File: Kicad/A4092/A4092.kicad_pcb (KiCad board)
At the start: 4 copper layers, 175.6 x 122.1 mm, 127 parts, among them CN1 Zorro3, J1 5749721-7, J2 5749721-7, J3 TO-LED, J4 TO-MB, J5 TO-A3000-LED, J6 TO-A3000-MB, J8 Conn_01x06_Pin, U1 SN74ABT16543DGGR, U10 DS21S07A, U11 DS21S07A, U12 DS21S07A, U13 W25X40CLSN, U2 SN74ABT16543DGGR, U3 SN74ABT16543DGGR, U4 SN74ABT16543DGGR, U5 74LVC07APW_118, U6 SN74ABT16245ADGGR, U7 AMS1117-3.3, U8 XC95144XL-TQ144, U9 LSI53C770 SCSI Host Controller, Y1 Abracon ACO-50MHz, Y2 Abracon ACO-40MHz

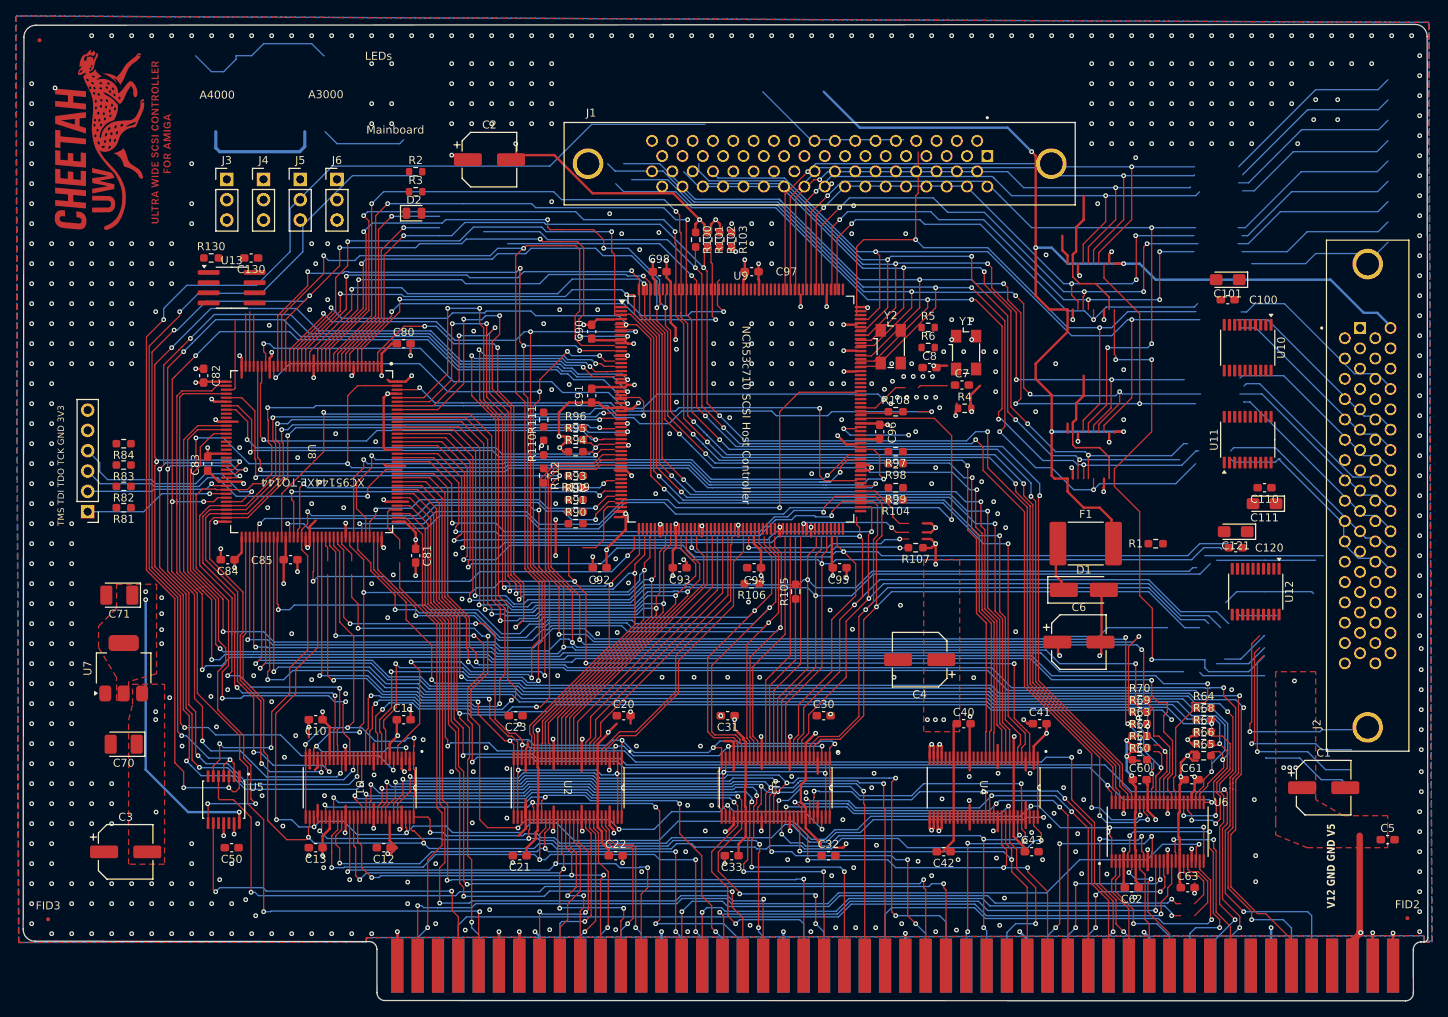
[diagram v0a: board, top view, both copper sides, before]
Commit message: Placement updates -SCSI moved south
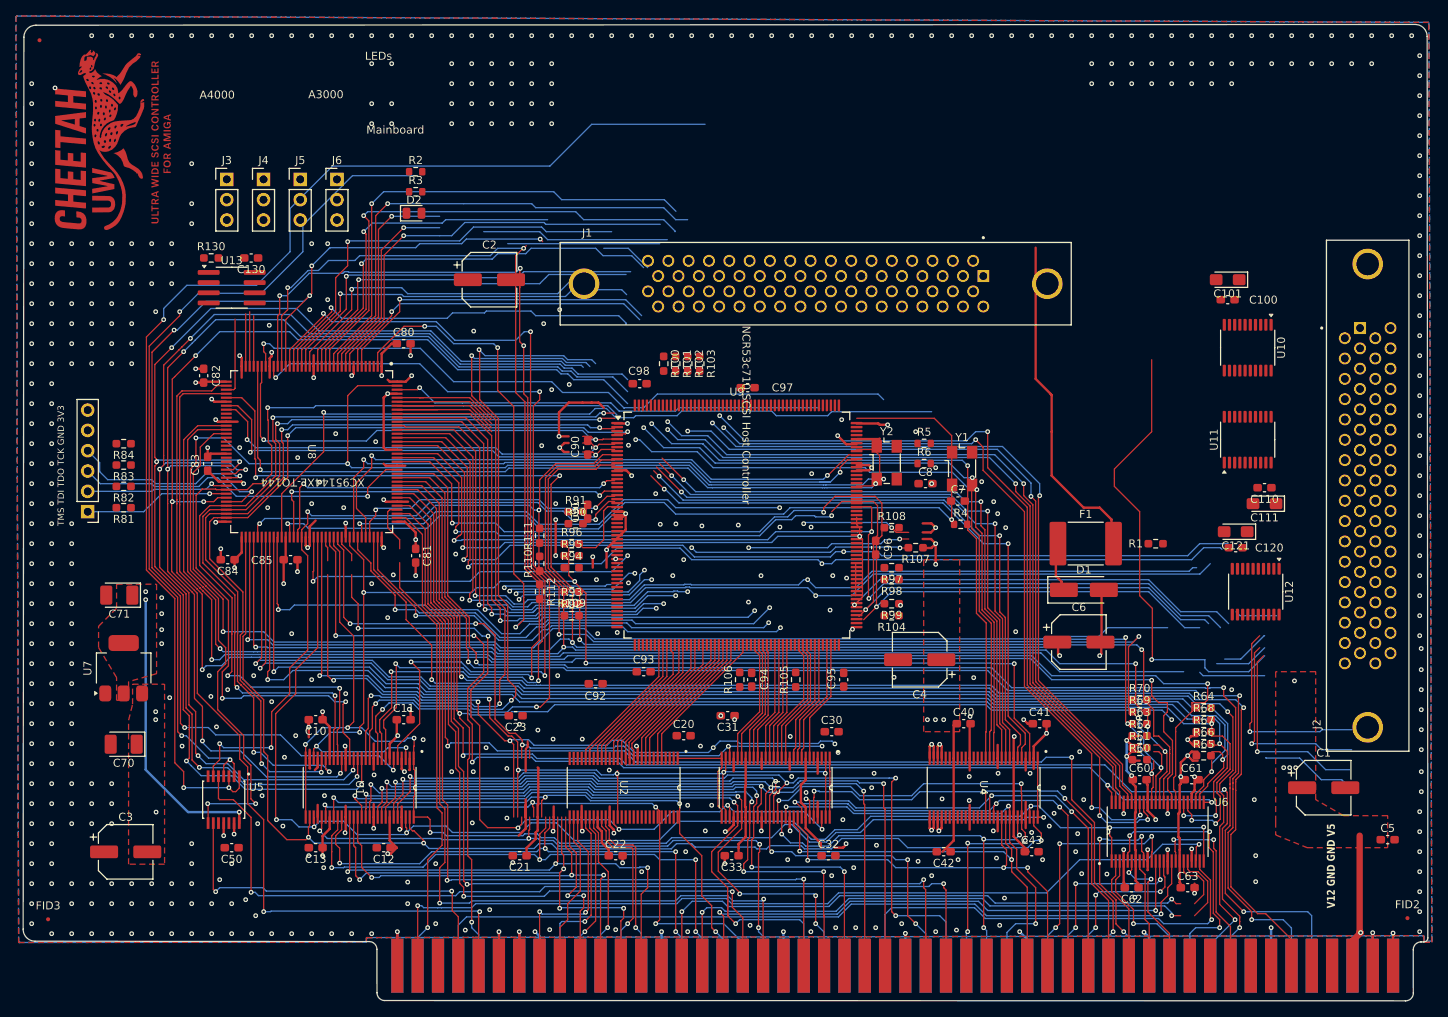
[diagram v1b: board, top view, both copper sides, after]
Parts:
- moved R100 16.0 mm to (129.0, 75.0)
- moved R101 16.0 mm to (130.5, 75.0)
- moved R102 16.0 mm to (132.0, 75.0)
- moved R103 16.0 mm to (133.5, 75.0)
- moved C2 15.0 mm to (107.2, 64.5)
- moved J1 15.0 mm to (148.0, 65.0)
- moved C7 14.5 mm to (165.8, 92.2)
- moved C8 14.5 mm to (161.7, 90.0)
- moved C90 14.5 mm to (119.5, 85.5)
- moved C91 14.5 mm to (119.5, 93.5)
- moved C92 14.5 mm to (120.5, 115.0)
- moved C96 14.5 mm to (155.5, 98.0)
- moved C97 14.5 mm to (139.5, 78.0)
- moved R104 14.5 mm to (157.5, 106.5)
- moved R108 14.5 mm to (157.5, 95.5)
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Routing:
- net (no net): track 393.0 -> 36.8 mm
- net SCDAT0: track 202.9 -> 0.00 mm, vias 6 -> 0
- net SCTRL_MSG: track 200.5 -> 0.00 mm, vias 8 -> 0
- net GND: track 471.6 -> 304.1 mm, vias 684 -> 550
- net SCDAT1: track 153.9 -> 0.00 mm, vias 4 -> 0
- net V5: track 585.5 -> 454.3 mm, vias 66 -> 53
- net SCDATP0: track 126.6 -> 0.00 mm, vias 6 -> 0
- net SCTRL_IO: track 119.2 -> 0.00 mm, vias 5 -> 0
- net SCTRL_REQ: track 110.0 -> 0.00 mm, vias 4 -> 0
- net SCSI_TERMPWR: track 148.3 -> 42.1 mm, vias 5 -> 0
- net SCTRL_SEL: track 105.8 -> 0.00 mm, vias 4 -> 0
- net SCTRL_RST: track 96.4 -> 0.00 mm, vias 4 -> 0
- net SCSI_BUSY: track 249.3 -> 153.4 mm, vias 5 -> 3
- net SCDAT4: track 94.2 -> 0.00 mm, vias 4 -> 0
- net CLK_50M: track 91.9 -> 0.00 mm
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
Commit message: CPLD Placement changes
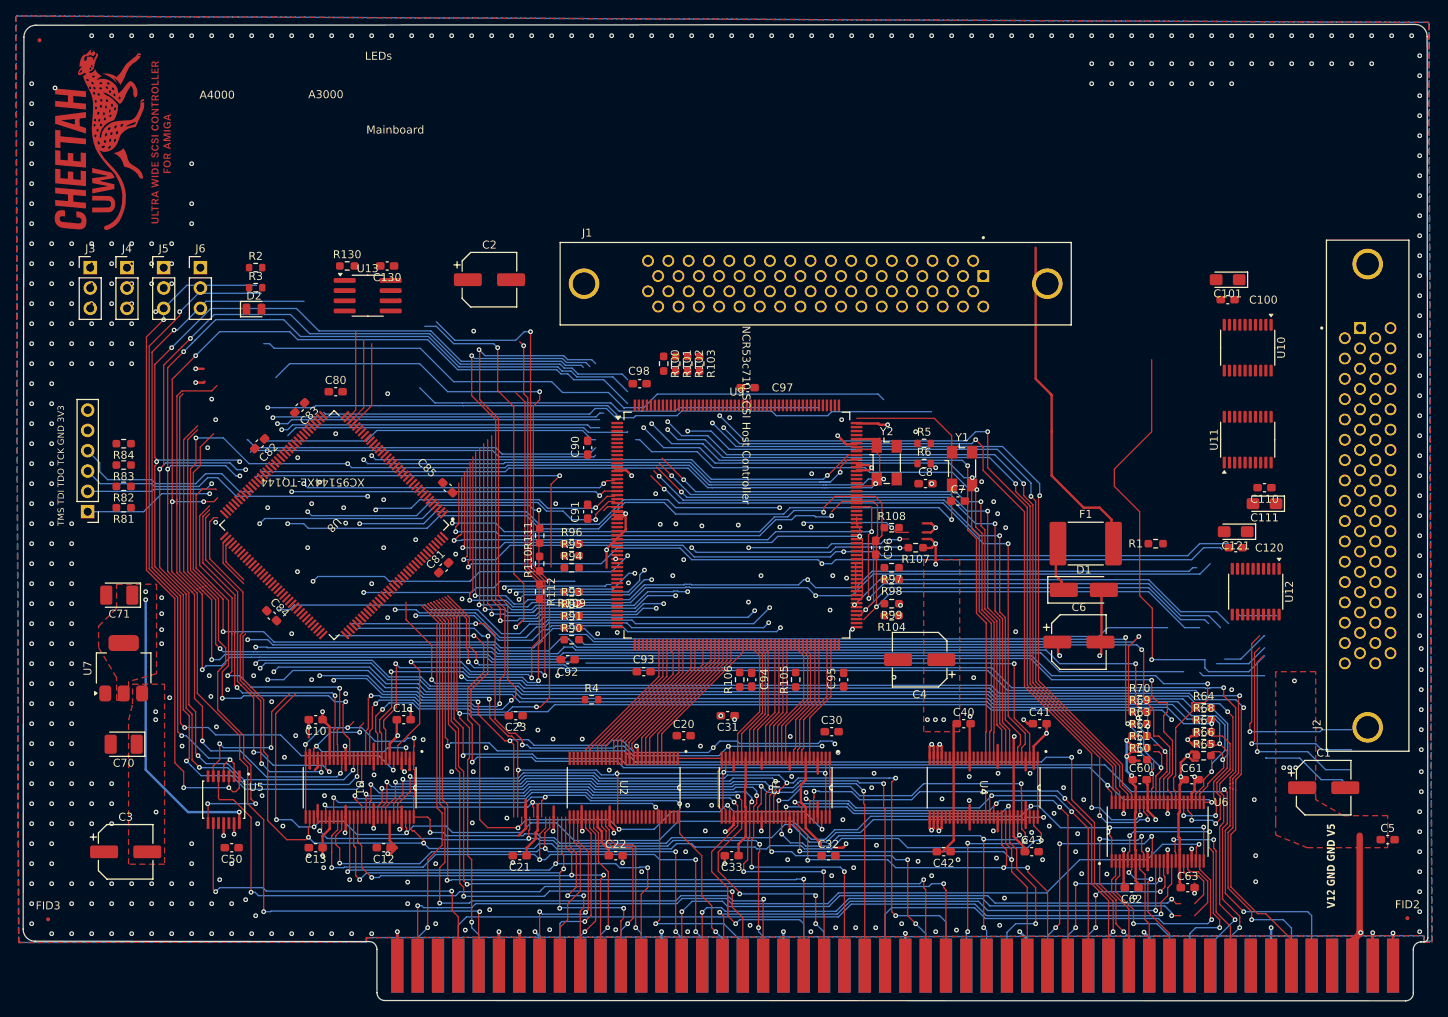
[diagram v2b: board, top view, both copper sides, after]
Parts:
- moved R4 51.1 mm to (120.0, 117.0)
- moved D2 23.3 mm to (77.8, 68.2)
- moved R2 23.3 mm to (78.0, 63.0)
- moved R3 23.3 mm to (78.0, 65.5)
- moved C85 21.6 mm to (102.0, 90.5), turned to -45 degrees
- moved J4 20.3 mm to (61.9, 63.0)
- moved J3 20.3 mm to (57.3, 63.0)
- moved J5 20.3 mm to (66.5, 63.0)
- moved J6 20.3 mm to (71.1, 63.0)
- moved C130 17.0 mm to (94.4, 62.8)
- moved R130 17.0 mm to (89.4, 62.8)
- moved U13 17.0 mm to (92.0, 66.5)
- moved R90 14.5 mm to (117.5, 109.5)
- moved R91 14.5 mm to (117.5, 108.0)
- moved C83 13.5 mm to (83.5, 80.5), turned to 45 degrees
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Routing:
- net GND: track 304.1 -> 478.5 mm, vias 550 -> 494
- net D2: track 146.2 -> 15.5 mm, vias 3 -> 0
- net SBR: track 95.4 -> 0.00 mm, vias 1 -> 0
- net V3_3: track 77.4 -> 159.1 mm, vias 12 -> 8
- net SLACK: track 75.8 -> 0.00 mm, vias 2 -> 0
- net SREG: track 74.6 -> 0.00 mm, vias 2 -> 0
- net SCSI_BUSY: track 153.4 -> 85.8 mm
- net MASTER: track 154.7 -> 88.4 mm, vias 7 -> 4
- net BERR: track 84.5 -> 18.7 mm, vias 4 -> 2
- net SCTRL_CD: track 0.00 -> 65.6 mm, vias 0 -> 2
- net A6: track 154.5 -> 92.5 mm, vias 3 -> 2
- net A7: track 152.6 -> 91.3 mm, vias 3 -> 2
- net A5: track 151.8 -> 90.5 mm, vias 3 -> 2
- net A31: track 105.1 -> 44.1 mm, vias 4 -> 2
- net A18: track 128.3 -> 67.6 mm, vias 4 -> 2
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
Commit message: Initial routing and signal clean up
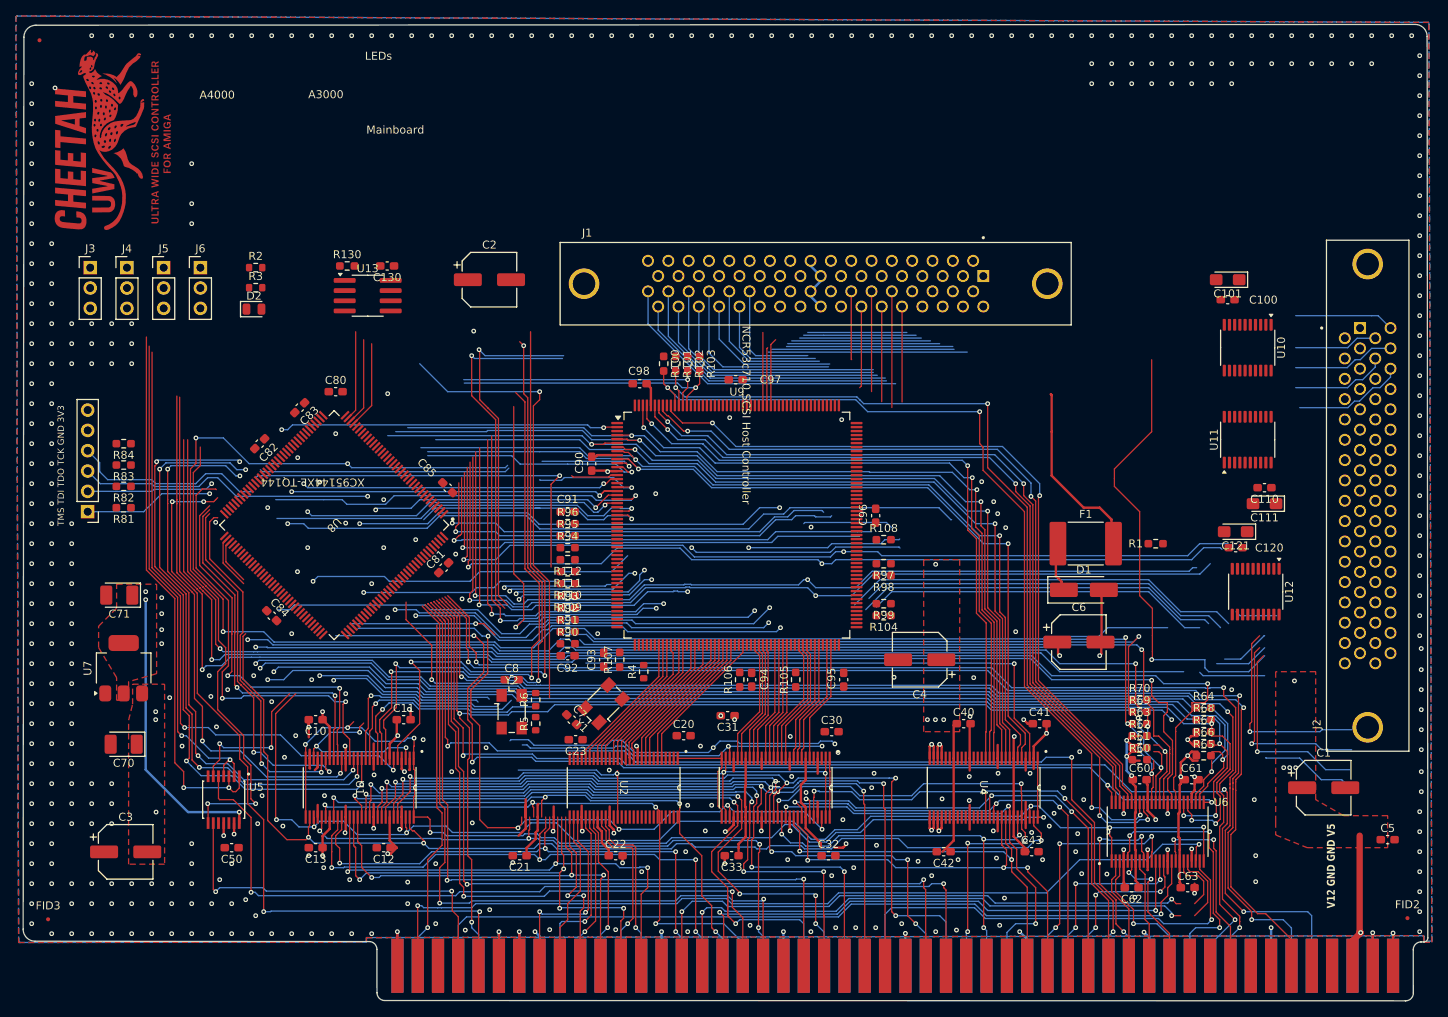
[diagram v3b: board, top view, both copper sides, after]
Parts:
- moved R5 59.9 mm to (113.0, 120.0), turned to 90 degrees
- moved C8 57.2 mm to (110.0, 114.5)
- moved R6 56.8 mm to (113.0, 117.0), turned to 90 degrees
- moved Y2 56.3 mm to (110.0, 118.5)
- moved C7 55.5 mm to (117.5, 119.5), turned to -45 degrees
- moved Y1 53.6 mm to (121.5, 117.5), turned to 135 degrees
- moved R107 39.6 mm to (123.5, 112.0), turned to 90 degrees
- moved C23 8.08 mm to (118.0, 122.0)
- moved R4 7.38 mm to (126.5, 113.5), turned to 90 degrees
- moved R111 5.70 mm to (117.0, 101.0), turned to 180 degrees
- moved R112 5.32 mm to (117.0, 99.5), turned to 180 degrees
- moved C93 5.22 mm to (121.5, 112.0), turned to -90 degrees
- moved R110 4.30 mm to (117.0, 102.5), turned to 180 degrees
- moved C96 4.00 mm to (155.5, 94.0), turned to 90 degrees
- moved R94 2.55 mm to (117.0, 98.0)
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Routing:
- net V3_3: track 159.1 -> 36.6 mm, vias 8 -> 5
- net GND: track 478.5 -> 356.7 mm, vias 494 -> 455
- net V5: track 458.8 -> 343.1 mm, vias 52 -> 30
- net BCLK: track 82.0 -> 0.00 mm
- net A27: track 137.3 -> 58.8 mm, vias 5 -> 4
- net A24: track 192.8 -> 114.6 mm, vias 7 -> 6
- net D1: track 186.5 -> 119.3 mm, vias 5 -> 3
- net IORST: track 154.1 -> 99.3 mm, vias 5 -> 4
- net SC0: track 51.4 -> 0.00 mm
- net Net-(U9B-GPIO0): track 0.00 -> 50.0 mm, vias 0 -> 1
- net PLD_READ: track 146.7 -> 96.7 mm, vias 4 -> 3
- net PLD_DS: track 80.9 -> 31.4 mm, vias 1 -> 0
- net SCDAT12: track 0.00 -> 46.5 mm
- net DP0: track 0.00 -> 45.9 mm
- net PLD_SIZ1: track 44.7 -> 0.00 mm
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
